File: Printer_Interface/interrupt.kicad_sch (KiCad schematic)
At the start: 15 parts, among them J3 IACK, J4 IRQ, U16 74HCT138, U17 INTERRUPT_GAL, U18 74HCT1G32, U19 74LVC1G08, U20 74LVC1G175, U21 74LVC1G74, U22 74LVC1G07

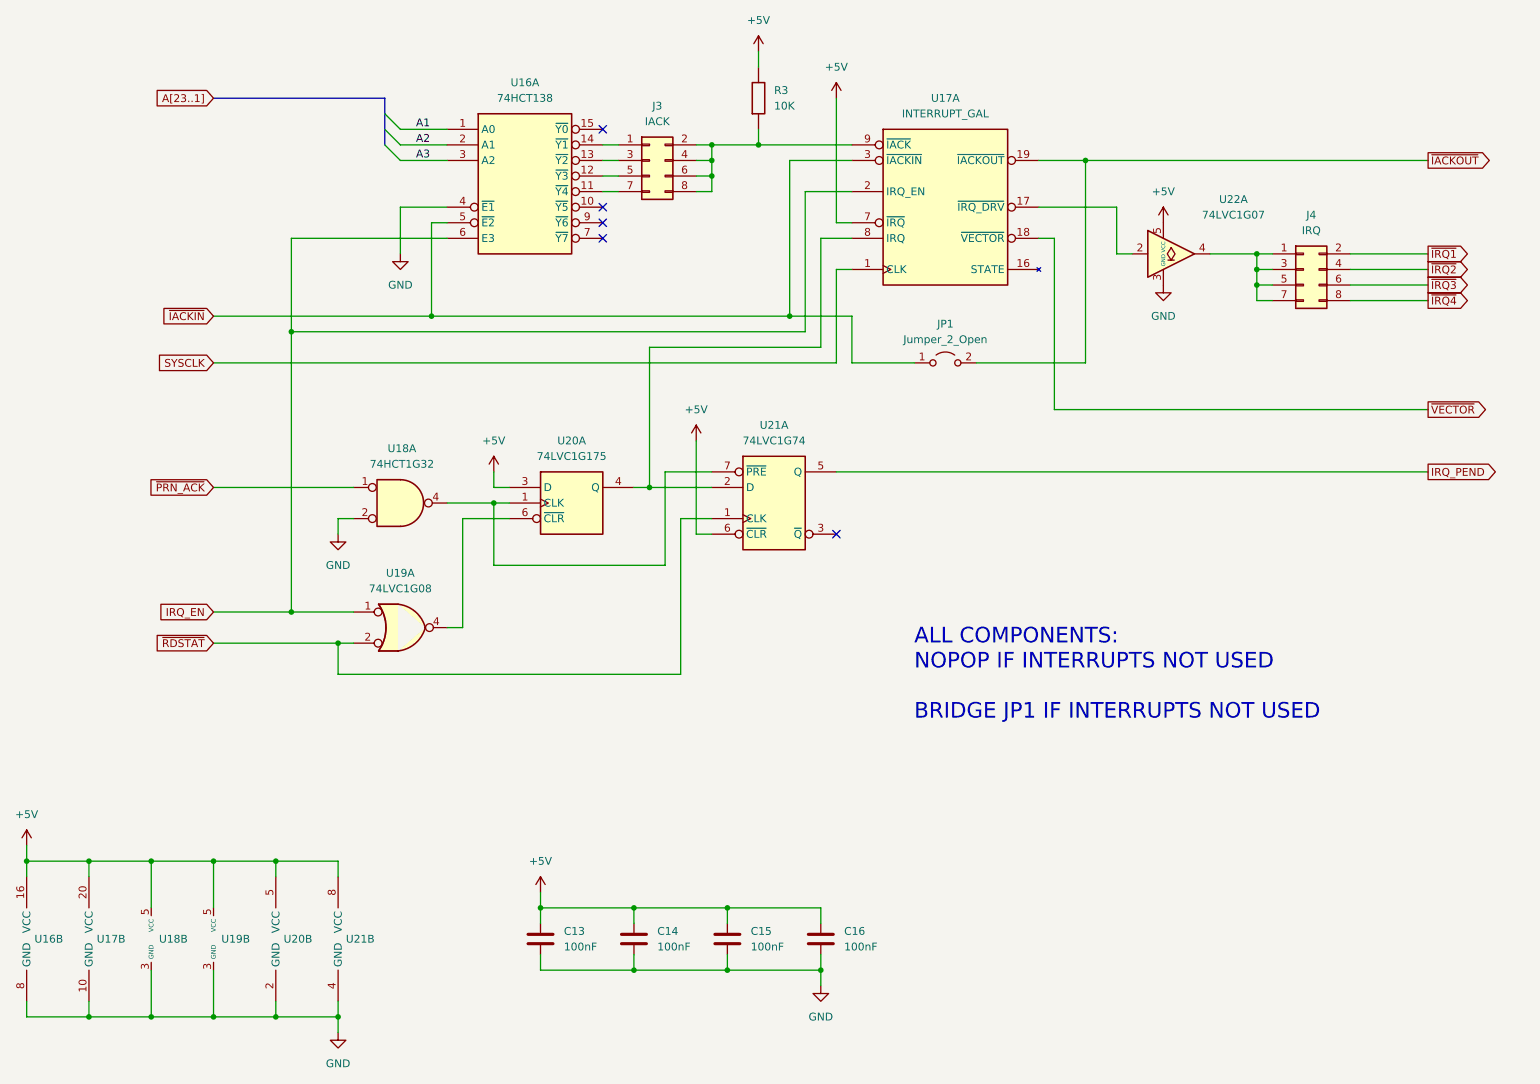
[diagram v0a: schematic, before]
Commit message: Routing complete, review time
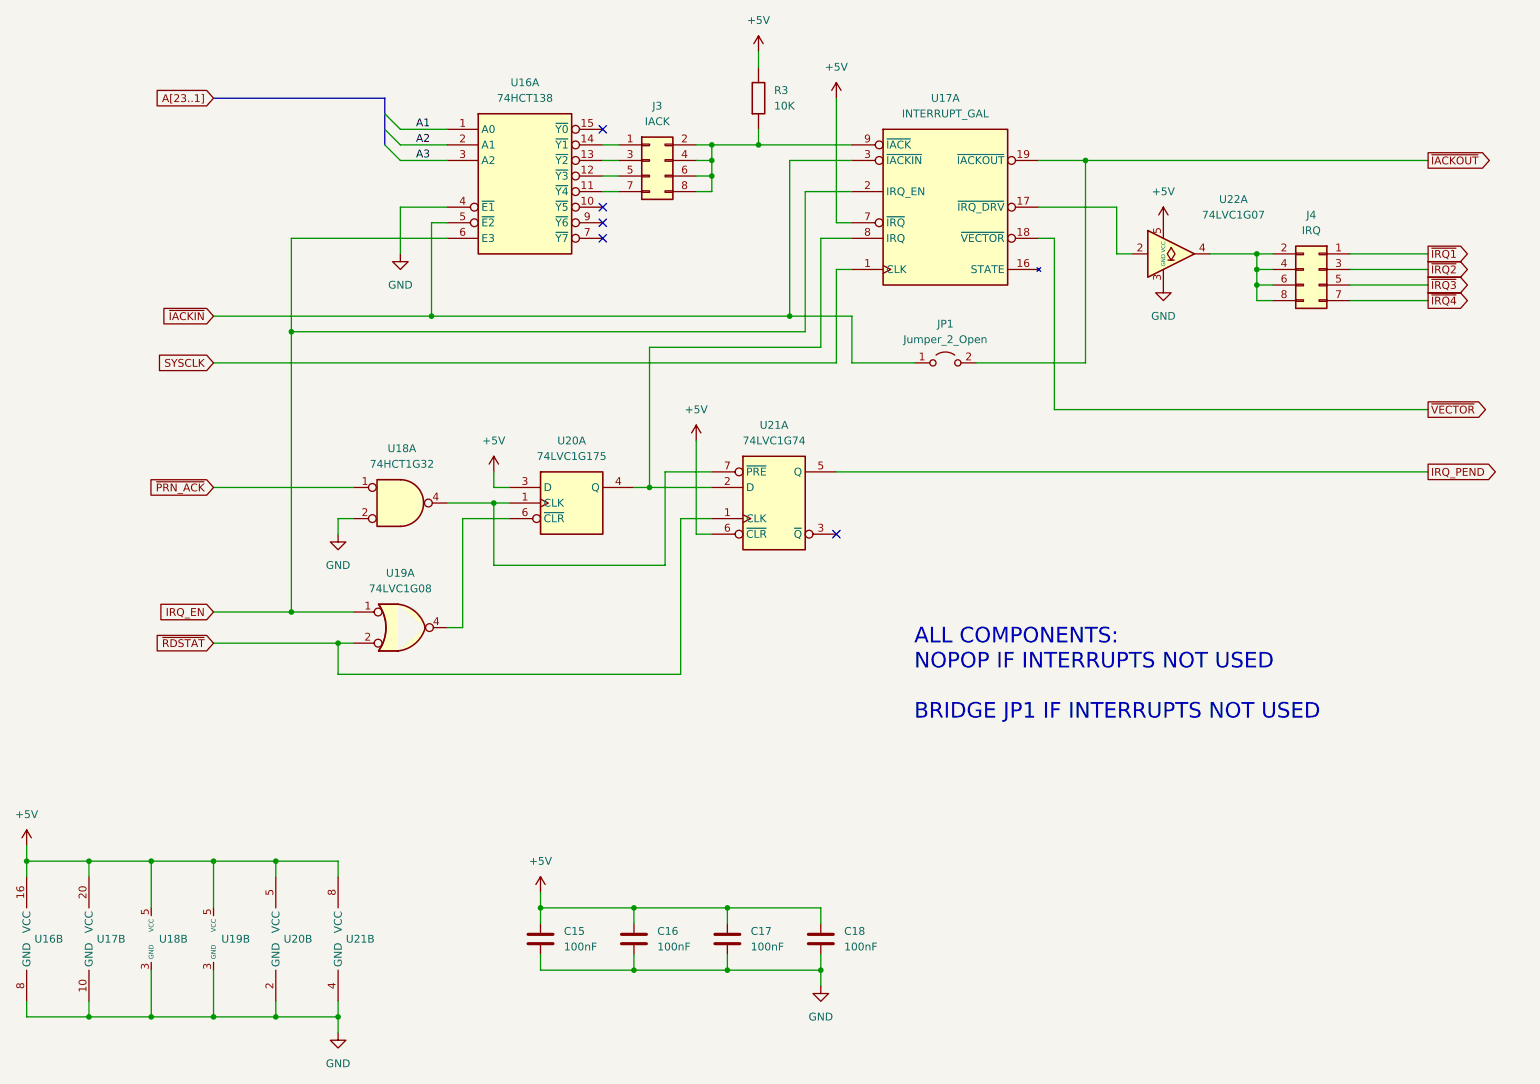
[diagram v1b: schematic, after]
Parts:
- renumbered C13 to C15, C14 to C16, C15 to C17, C16 to C18
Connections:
- net ~{IRQ1}: now also J4.1 (Pin_1); no longer J4.2 (Pin_2)
- net ~{IRQ2}: now also J4.3 (Pin_3); no longer J4.4 (Pin_4)
- net ~{IRQ3}: now also J4.5 (Pin_5); no longer J4.6 (Pin_6)
- net ~{IRQ4}: now also J4.7 (Pin_7); no longer J4.8 (Pin_8)
- new net: J4.2 (Pin_2), J4.4 (Pin_4), J4.6 (Pin_6), J4.8 (Pin_8), U22.4

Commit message: ERC/DRC pass, clean for the most part
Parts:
- renumbered C15 to C16, C16 to C17, C17 to C18, C18 to C19
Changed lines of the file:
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@@
 			)
 		)
-		(property "Description" ""
+		(property "Description" "Power symbol creates a global label with name \"+5V\""
 			(at 129.54 91.44 0)
 			(effects
@@
 			)
 		)
-		(property "Description" ""
+		(property "Description" "Power symbol creates a global label with name \"GND\" , ground"
 			(at 71.12 187.96 0)
 			(effects
@@
 			)
 		)
-		(property "Description" ""
+		(property "Description" "Power symbol creates a global label with name \"GND\" , ground"
 			(at 71.12 106.68 0)
 			(effects
@@
 			)
 		)
-		(property "Description" ""
+		(property "Description" "Power symbol creates a global label with name \"+5V\""
 			(at 96.52 96.52 0)
 			(effects
@@
 			)
 		)
-		(property "Description" ""
+		(property "Description" "Power symbol creates a global label with name \"+5V\""
 			(at 104.14 165.1 0)
 			(effects
@@
 			)
 		)
-		(property "Description" ""
+		(property "Description" "Single 2-input AND gate"
 			(at 81.28 121.92 0)
 			(effects
@@
 			)
 		)
-		(property "Description" ""
+		(property "Description" "Power symbol creates a global label with name \"GND\" , ground"
 			(at 81.28 60.96 0)
 			(effects
@@
 		(dnp no)
 		(fields_autoplaced yes)
-		(property "Reference" "C17"
+		(property "Reference" "C18"
 			(at 138.43 171.4499 0)
 			(effects
@@
 			(project "Printer_Interface"
 				(path "/75b66dbb-7202-4875-8695-2c14dee692f0/5e3df452-5717-4bd3-bb16-2ac0410dccdc"
-					(reference "C17")
+					(reference "C18")
 					(unit 1)
 				)
@@
 			)
 		)
-		(property "Description" ""
+		(property "Description" "Power symbol creates a global label with name \"GND\" , ground"
 			(at 149.86 180.34 0)
 			(effects
@@
 		(dnp no)
 		(fields_autoplaced yes)
-		(property "Reference" "C16"
+		(property "Reference" "C17"
 			(at 123.19 171.4499 0)
 			(effects
@@
 			(project "Printer_Interface"
 				(path "/75b66dbb-7202-4875-8695-2c14dee692f0/5e3df452-5717-4bd3-bb16-2ac0410dccdc"
-					(reference "C16")
+					(reference "C17")
 					(unit 1)
 				)
@@
 		(dnp no)
 		(fields_autoplaced yes)
-		(property "Reference" "C15"
+		(property "Reference" "C16"
 			(at 107.95 171.4499 0)
 			(effects
@@
 			(project "Printer_Interface"
 				(path "/75b66dbb-7202-4875-8695-2c14dee692f0/5e3df452-5717-4bd3-bb16-2ac0410dccdc"
-					(reference "C15")
+					(reference "C16")
 					(unit 1)
 				)
@@
 			)
 		)
-		(property "Description" ""
+		(property "Description" "Single 2-input OR gate"
 			(at 40.64 172.72 0)
 			(effects
@@
 			)
 		)
-		(property "Description" ""
+		(property "Description" "Power symbol creates a global label with name \"+5V\""
 			(at 139.7 27.94 0)
 			(effects
@@
 		(dnp no)
 		(fields_autoplaced yes)
-		(property "Reference" "C18"
+		(property "Reference" "C19"
 			(at 153.67 171.4499 0)
 			(effects
@@
 			(project "Printer_Interface"
 				(path "/75b66dbb-7202-4875-8695-2c14dee692f0/5e3df452-5717-4bd3-bb16-2ac0410dccdc"
-					(reference "C18")
+					(reference "C19")
 					(unit 1)
 				)
@@
 			)
 		)
-		(property "Description" ""
+		(property "Description" "Single D-type flip-flop with set and reset; positive edge trigger"
 			(at 71.12 172.72 0)
 			(effects
@@
 			)
 		)
-		(property "Description" ""
+		(property "Description" "Power symbol creates a global label with name \"+5V\""
 			(at 205.74 55.88 0)
 			(effects
@@
 			)
 		)
-		(property "Description" ""
+		(property "Description" "Power symbol creates a global label with name \"+5V\""
 			(at 20.32 157.48 0)
 			(effects
@@
 			)
 		)
-		(property "Description" ""
+		(property "Description" "Generic connector, double row, 02x04, odd/even pin numbering scheme (row 1 odd numbers, row 2 even numbers), script generated (kicad-library-utils/schlib/autogen/connector/)"
 			(at 231.14 63.5 0)
 			(effects
@@
 			)
 		)
-		(property "Description" ""
+		(property "Description" "Single D-type flip-flop with set and reset; positive edge trigger"
 			(at 142.24 101.6 0)
 			(effects
@@
 			)
 		)
-		(property "Description" ""
+		(property "Description" "Power symbol creates a global label with name \"+5V\""
 			(at 152.4 35.56 0)
 			(effects
@@
 			)
 		)
-		(property "Description" ""
+		(property "Description" "Buffer with open-drain output"
 			(at 205.74 60.96 0)
 			(effects
@@
 			)
 		)
-		(property "Description" ""
+		(property "Description" "Buffer with open-drain output"
 			(at 205.74 60.96 0)
 			(effects
@@
 			)
 		)
-		(property "Description" ""
+		(property "Description" "Single 2-input AND gate"
 			(at 50.8 172.72 0)
 			(effects
@@
 			)
 		)
-		(property "Description" ""
+		(property "Description" "Power symbol creates a global label with name \"GND\" , ground"
 			(at 205.74 66.04 0)
 			(effects
@@
 			)
 		)
-		(property "Description" ""
+		(property "Description" "Jumper, 2-pole, open"
 			(at 170.18 78.74 0)
 			(effects
@@
 			)
 		)
-		(property "Description" ""
+		(property "Description" "Single D-type flip-flop with reset; positive edge trigger"
 			(at 109.22 101.6 0)
 			(effects
@@
 			)
 		)
-		(property "Description" ""
+		(property "Description" "Single 2-input OR gate"
 			(at 81.28 101.6 0)
 			(effects
@@
 			)
 		)
-		(property "Description" ""
+		(property "Description" "3-to-8 line decoder/demultiplexer; inverting"
 			(at 101.6 48.26 0)
 			(effects
@@
 			)
 		)
-		(property "Description" ""
+		(property "Description" "3-to-8 line decoder/demultiplexer; inverting"
 			(at 20.32 172.72 0)
 			(effects
@@
 			)
 		)
-		(property "Description" ""
+		(property "Description" "Single D-type flip-flop with reset; positive edge trigger"
 			(at 60.96 172.72 0)
 			(effects
@@
 			)
 		)
-		(property "Description" ""
+		(property "Description" "Generic connector, double row, 02x04, odd/even pin numbering scheme (row 1 odd numbers, row 2 even numbers), script generated (kicad-library-utils/schlib/autogen/connector/)"
 			(at 121.92 45.72 0)
 			(effects

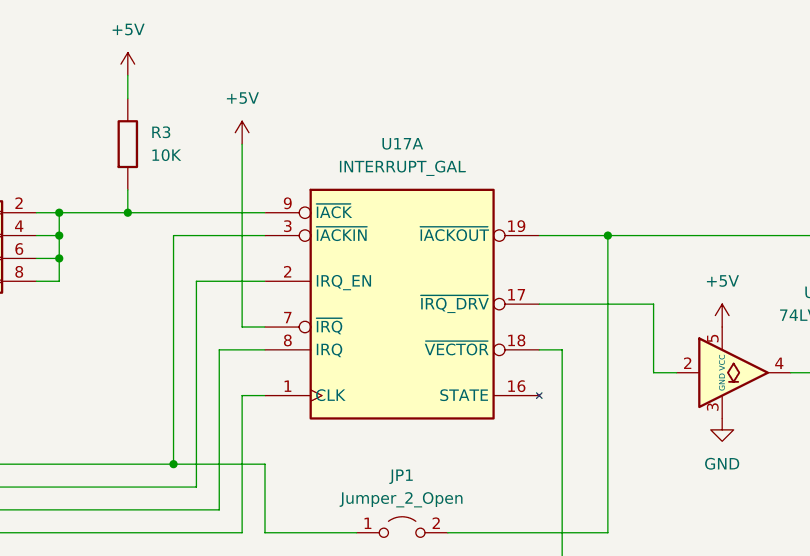
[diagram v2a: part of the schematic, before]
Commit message: Interrupt GAL signal optimisations
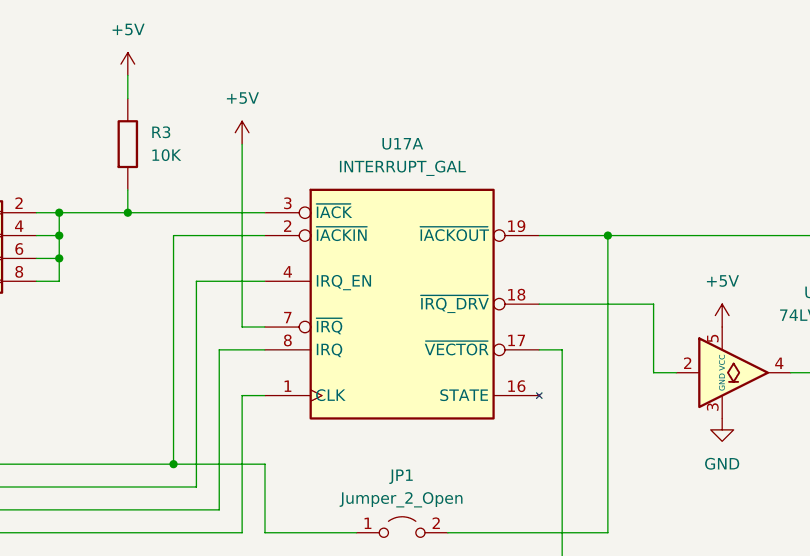
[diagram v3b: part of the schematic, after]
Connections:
- net IRQ_EN: now also U17.4 (IRQ_EN); no longer U17.2 (IRQ_EN)
- net ~{IACKIN}: now also U17.2 (~{IACKIN}); no longer U17.3 (~{IACKIN})
- net ~{VECTOR}: now also U17.17 (~{VECTOR}); no longer U17.18 (~{VECTOR})
- net at J3.2 (Pin_2), J3.4 (Pin_4), J3.6 (Pin_6)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: now also U17.3 (~{IACK}); no longer U17.9 (~{IACK})
- net at U22.2: now also U17.18 (~{IRQ_DRV}); no longer U17.17 (~{IRQ_DRV})
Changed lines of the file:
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@@
 	(title_block
 		(title "INTERRUPT LOGIC")
-		(date "2024-02-22")
+		(date "2024-03-04")
 		(rev "1")
 		(company "(C) TOM STOREY")
@@
 		(pin "19"
 		)
-		(pin "2"
+		(pin "4"
 		)
 		(pin "3"
@@
 		(pin "8"
 		)
-		(pin "9"
+		(pin "2"
 		)
 		(pin "10"
@@
 		(pin "19"
 		)
-		(pin "2"
+		(pin "4"
 		)
 		(pin "3"
@@
 		(pin "8"
 		)
-		(pin "9"
+		(pin "2"
 		)
 		(pin "10"

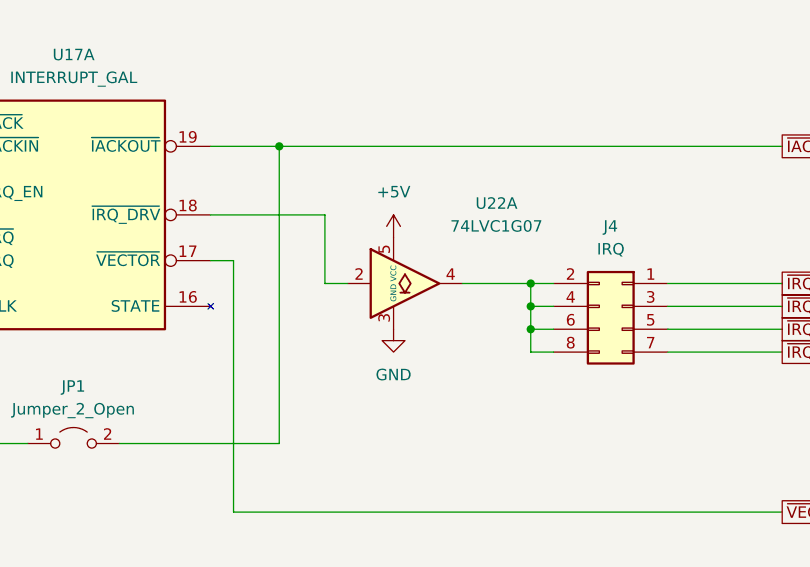
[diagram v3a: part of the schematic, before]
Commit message: Incorporate symbol fixes
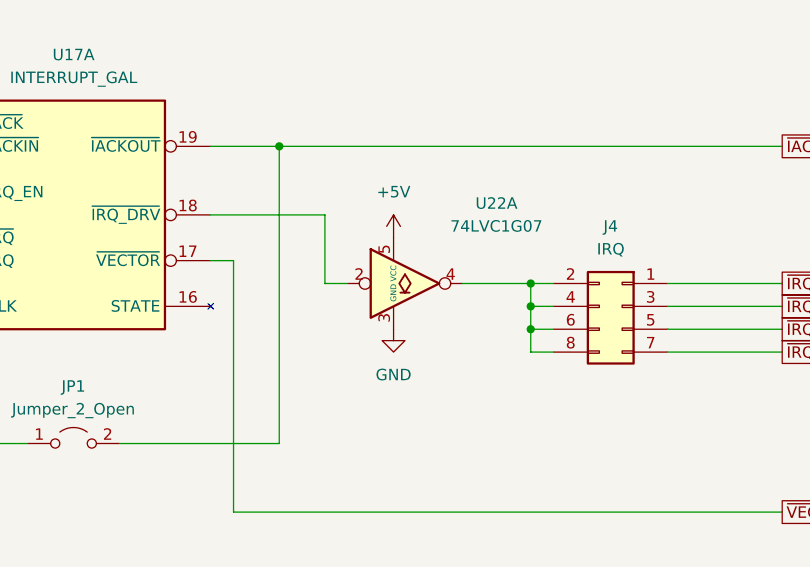
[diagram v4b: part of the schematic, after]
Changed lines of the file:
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@@
 		(at 205.74 60.96 0)
 		(unit 1)
+		(convert 2)
 		(exclude_from_sim no)
 		(in_bom yes)
